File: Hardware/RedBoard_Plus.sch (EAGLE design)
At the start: 80 parts, among them IC3 LM1117, J2 ISP, J3 5.5x2.1mm Barrel, J4 QWIIC_RIGHT_ANGLE, J5 USB Female Type C Connector, Q1 20V/4.2A/52mΩ/1.4W, Q2 310mA/60V/1.6Ω, Q3 310mA/60V/1.6Ω, U3 3.3V, U4 ATMEGA328P_TQFP, U5 CH340C, Y1 16MHz

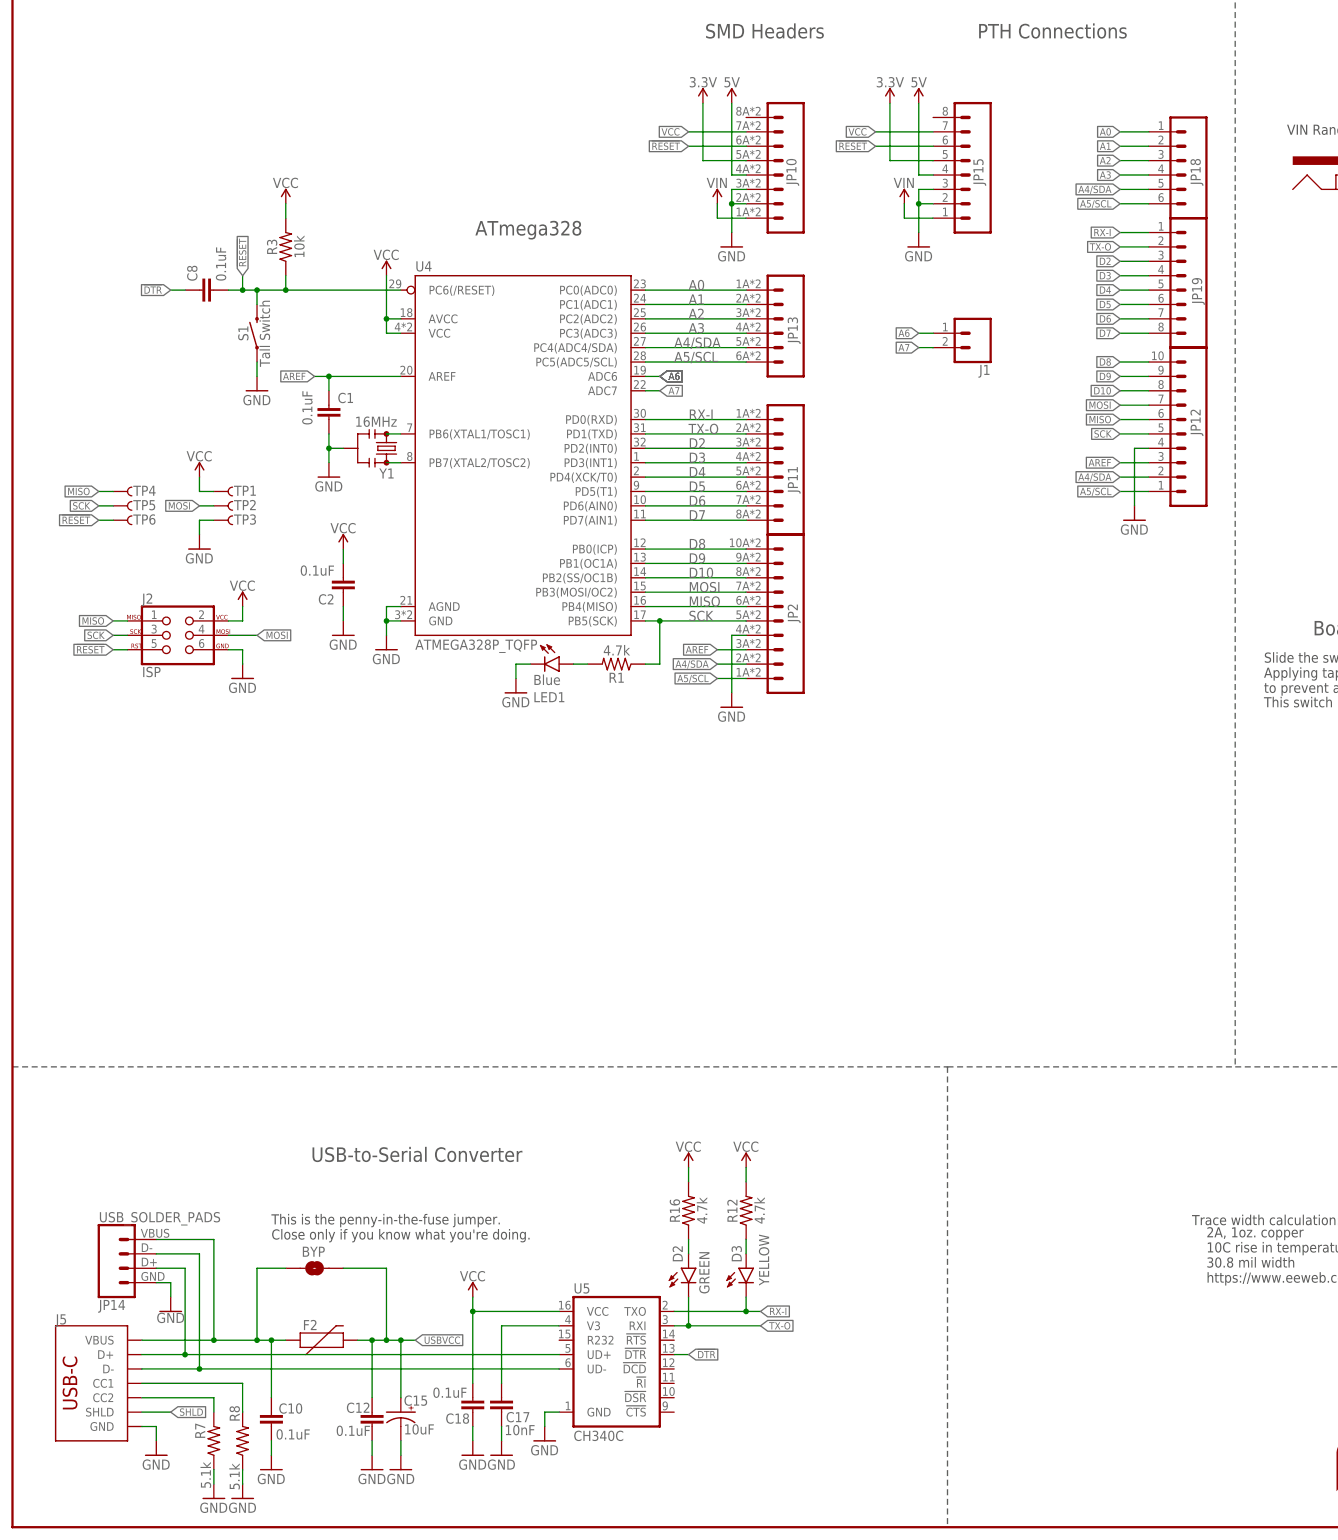
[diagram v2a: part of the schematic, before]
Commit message: Switch CH340C for CH340G with external oscillator
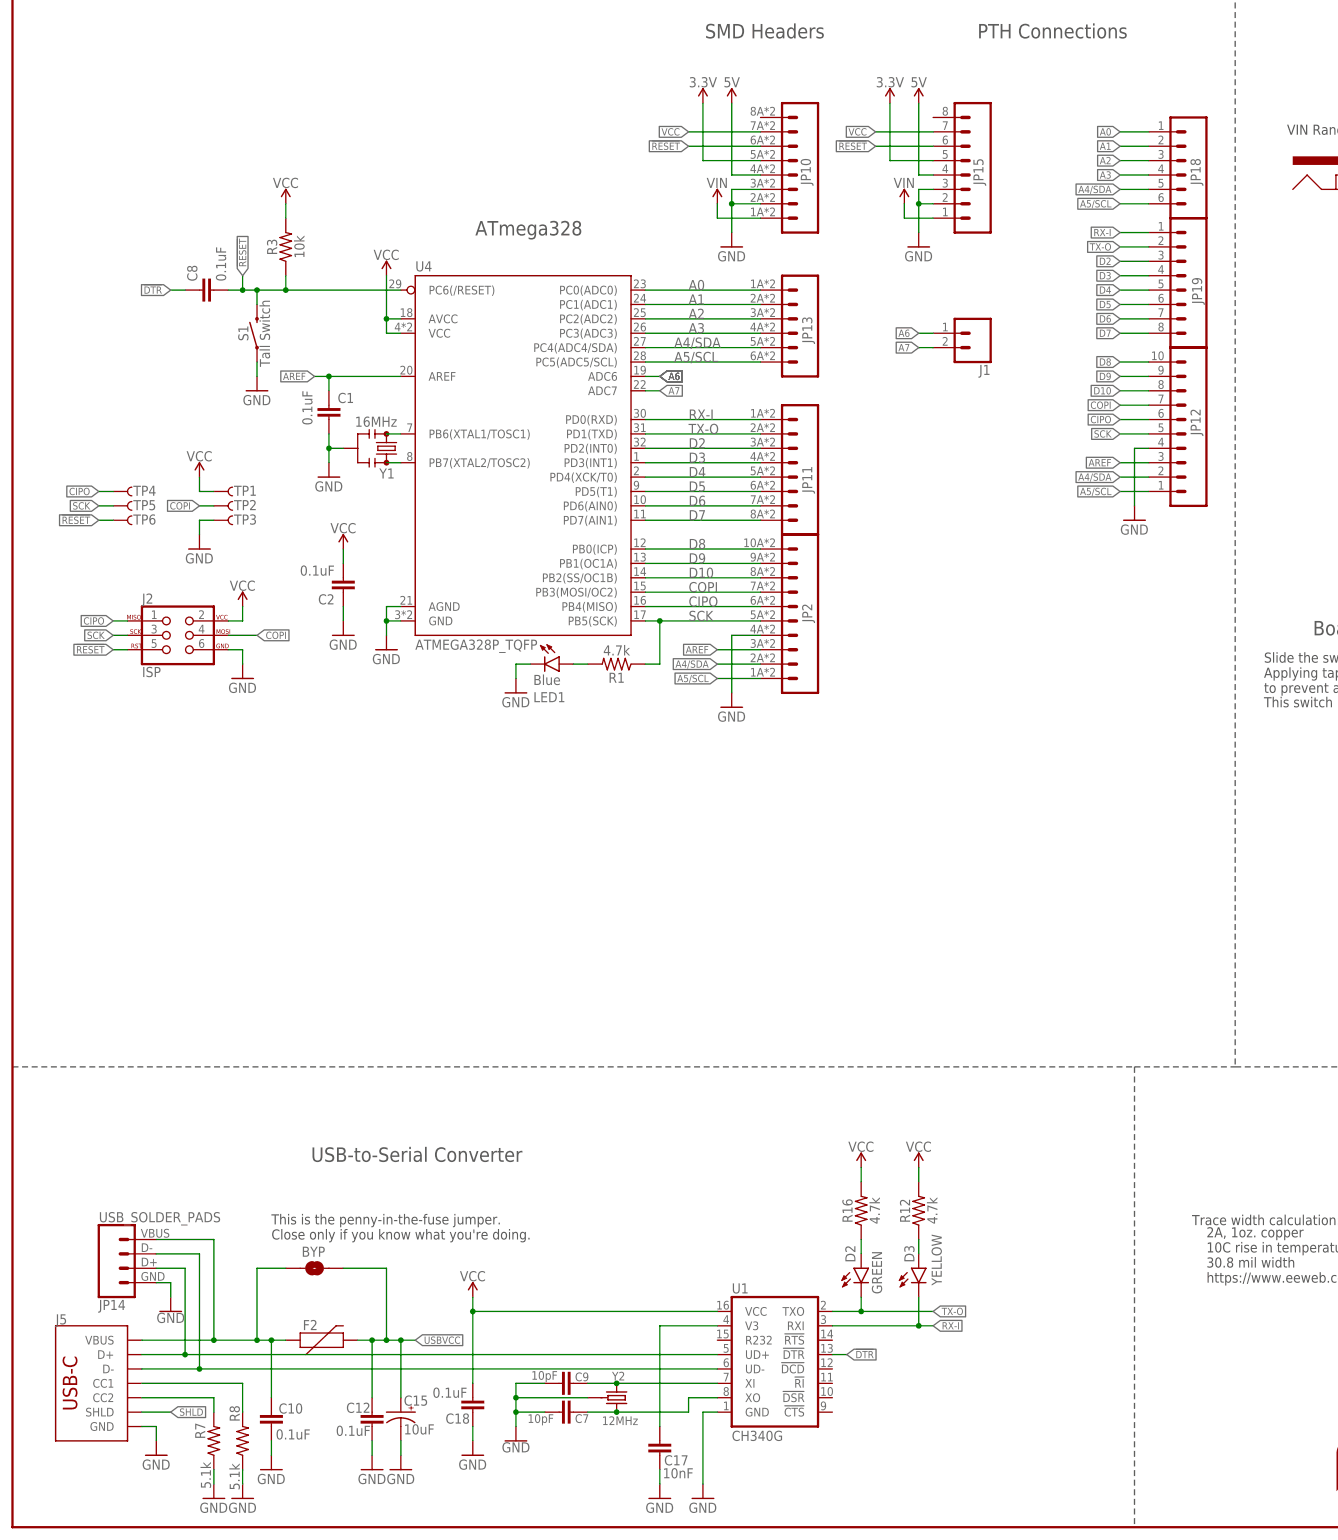
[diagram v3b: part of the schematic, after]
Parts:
- removed U5: CH340C, SparkFun-IC-Comms:CH340C
- added C7, C9: 10pF, SparkFun-Capacitors:10PF-0603-50V-5%
- added U1: CH340G, SparkFun-IC-Comms:CH340GSMD
- added Y2: 12MHz, SparkFun-Clocks:CRYSTAL-GROUNDEDSMD-3.2X2.5
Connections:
- net MISO renamed CIPO
- net MOSI renamed COPI
- removed net !DTR: C8.1, U5.!DTR
- new net !DTR!: C8.1, U1.!DTR
- new net N$10: C7.1, U1.XO, Y2.2
- new net N$8: C9.1, U1.XI, Y2.1
- net D+: now also U1.UD+; no longer U5.UD+
- net D-: now also U1.UD-; no longer U5.UD-
- net GND: now also C7.2, C9.2, U1.GND, Y2.GND; no longer U5.GND
- net N$6: now also U1.V3; no longer U5.V3
- net RX-I: now also U1.RXI; no longer U5.TXO
- net TX-O: now also U1.TXO; no longer U5.RXI
- net VCC: now also U1.VCC; no longer U5.VCC
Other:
- moved on the sheet: C17, D2, D3, JP10, JP13, JP2, R12, R16

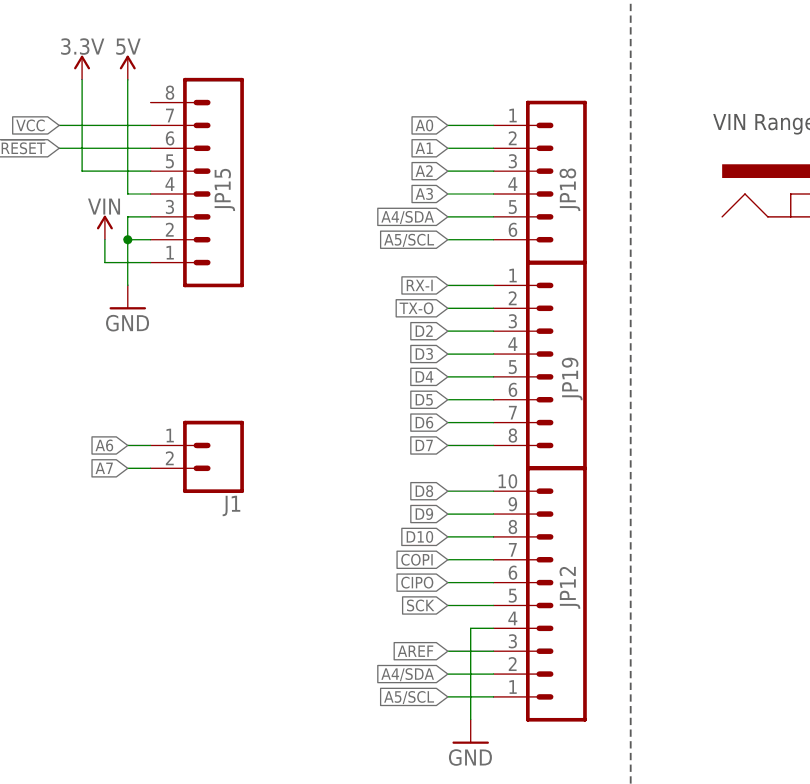
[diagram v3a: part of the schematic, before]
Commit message: Add "DNP" to headers on schematic
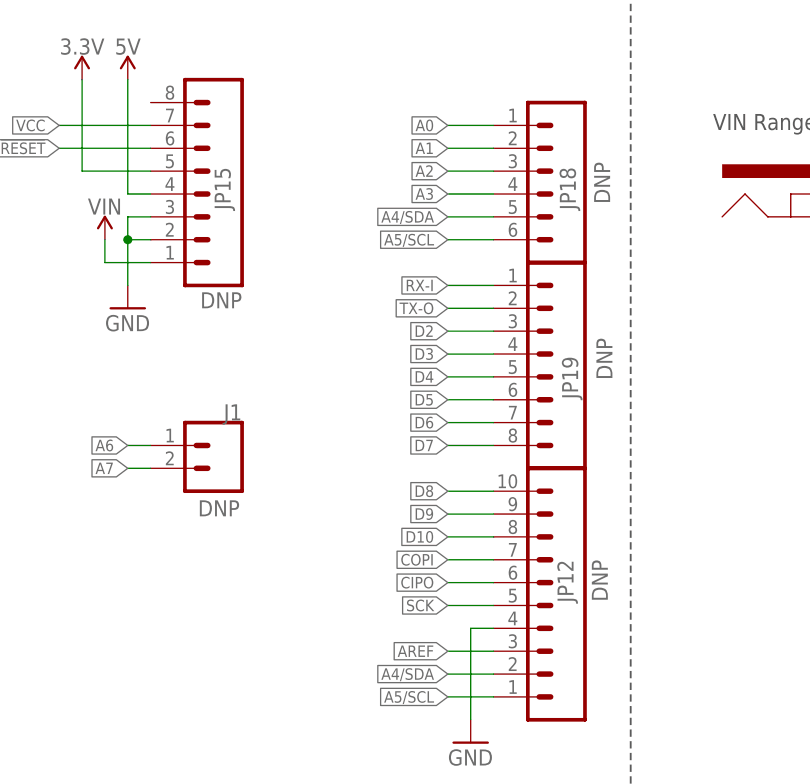
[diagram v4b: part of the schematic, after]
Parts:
- J1, JP15, JP18, JP19: value (none) -> DNP
- JP12: value M10NO_SILK -> DNP
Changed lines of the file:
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@@
 <part name="S2" library="SparkFun-Switches" deviceset="SWITCH-DPDT" device="-SMD-AYZ0202"/>
 <part name="FRAME1" library="SparkFun-Aesthetics" deviceset="FRAME-LEDGER" device=""/>
-<part name="JP12" library="SparkFun-Connectors" deviceset="M10" device="NO_SILK" value="M10NO_SILK">
+<part name="JP12" library="SparkFun-Connectors" deviceset="M10" device="NO_SILK" value="DNP">
 <attribute name="PROD_ID" value="CONN-11219"/>
 </part>
-<part name="JP15" library="SparkFun-Connectors" deviceset="M08" device="NO_SILK">
+<part name="JP15" library="SparkFun-Connectors" deviceset="M08" device="NO_SILK" value="DNP">
 <attribute name="PROD_ID" value="CONN-10204"/>
 </part>
@@
 <part name="SUPPLY1" library="SparkFun-PowerSymbols" deviceset="5V" device=""/>
 <part name="SUPPLY4" library="SparkFun-PowerSymbols" deviceset="VIN" device=""/>
-<part name="JP18" library="SparkFun-Connectors" deviceset="M06" device="NO_SILK">
+<part name="JP18" library="SparkFun-Connectors" deviceset="M06" device="NO_SILK" value="DNP">
 <attribute name="PROD_ID" value="CONN-10203"/>
 </part>
 <part name="GND36" library="SparkFun-PowerSymbols" deviceset="GND" device=""/>
-<part name="JP19" library="SparkFun-Connectors" deviceset="CONN_08" device="NO_SILK_FEMALE_PTH"/>
+<part name="JP19" library="SparkFun-Connectors" deviceset="CONN_08" device="NO_SILK_FEMALE_PTH" value="DNP"/>
 <part name="SUPPLY9" library="SparkFun-PowerSymbols" deviceset="3.3V" device=""/>
 <part name="GND9" library="SparkFun-PowerSymbols" deviceset="GND" device=""/>
-<part name="J1" library="SparkFun-Connectors" deviceset="CONN_02" device="1X02_NO_SILK"/>
+<part name="J1" library="SparkFun-Connectors" deviceset="CONN_02" device="1X02_NO_SILK" value="DNP"/>
 <part name="FD1" library="SparkFun-Aesthetics" deviceset="FIDUCIAL" device="1X2"/>
 <part name="FD2" library="SparkFun-Aesthetics" deviceset="FIDUCIAL" device="1X2"/>
@@
 </instance>
 <instance part="JP12" gate="G$1" x="210.82" y="200.66" smashed="yes" rot="MR0">
-<attribute name="NAME" x="209.804" y="192.786" size="1.778" layer="95" font="vector" rot="R90"/>
 <attribute name="PROD_ID" x="210.82" y="200.66" size="1.778" layer="96" rot="MR0" display="off"/>
+<attribute name="VALUE" x="213.36" y="198.12" size="1.778" layer="96" font="vector" rot="MR270"/>
+<attribute name="NAME" x="209.55" y="198.12" size="1.778" layer="95" font="vector" rot="MR270"/>
 </instance>
 <instance part="JP15" gate="G$1" x="167.64" y="238.76" smashed="yes" rot="MR0">
 <attribute name="PROD_ID" x="167.64" y="238.76" size="1.778" layer="96" rot="MR0" display="off"/>
-<attribute name="VALUE" x="172.72" y="226.06" size="1.778" layer="96" rot="MR0"/>
+<attribute name="VALUE" x="172.72" y="226.06" size="1.778" layer="96" font="vector" rot="MR0"/>
 <attribute name="NAME" x="171.45" y="236.982" size="1.778" layer="95" font="vector" rot="R90"/>
 </instance>
@@
 <instance part="JP18" gate="G$1" x="205.74" y="241.3" smashed="yes" rot="R180">
 <attribute name="PROD_ID" x="205.74" y="241.3" size="1.778" layer="96" rot="R180" display="off"/>
-<attribute name="VALUE" x="210.82" y="251.46" size="1.778" layer="96" rot="R180"/>
+<attribute name="VALUE" x="211.836" y="242.316" size="1.778" layer="96" font="vector" rot="R270"/>
 <attribute name="NAME" x="209.804" y="236.982" size="1.778" layer="95" font="vector" rot="R90"/>
 </instance>
@@
 </instance>
 <instance part="JP19" gate="G$1" x="205.74" y="220.98" smashed="yes" rot="R180">
-<attribute name="VALUE" x="210.82" y="233.426" size="1.778" layer="96" font="vector" rot="R180"/>
+<attribute name="VALUE" x="212.09" y="222.758" size="1.778" layer="96" font="vector" rot="R270"/>
 <attribute name="NAME" x="208.28" y="220.726" size="1.778" layer="95" font="vector" rot="R270"/>
 </instance>
@@
 </instance>
 <instance part="J1" gate="G$1" x="170.18" y="210.82" smashed="yes" rot="R180">
-<attribute name="VALUE" x="172.72" y="215.646" size="1.778" layer="96" font="vector" rot="R180"/>
-<attribute name="NAME" x="172.72" y="205.232" size="1.778" layer="95" font="vector" rot="R180"/>
+<attribute name="VALUE" x="172.466" y="204.724" size="1.778" layer="96" font="vector" rot="R180"/>
+<attribute name="NAME" x="172.72" y="215.392" size="1.778" layer="95" font="vector" rot="R180"/>
 </instance>
 <instance part="FD1" gate="G$1" x="424.18" y="17.78" smashed="yes"/>

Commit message: QC Double check changes
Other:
- note added: "Revised By: Priyanka Makin"
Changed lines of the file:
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@@
 <text x="183.642" y="264.16" size="2.54" layer="97" font="vector" align="center">PTH Connections</text>
 <text x="132.842" y="264.16" size="2.54" layer="97" font="vector" align="center">SMD Headers</text>
+<text x="375.92" y="5.842" size="1.778" layer="94" font="vector">Revised By: Priyanka Makin</text>
 </plain>
 <instances>
